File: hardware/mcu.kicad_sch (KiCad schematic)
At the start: 10 parts, among them U1 RP2350B

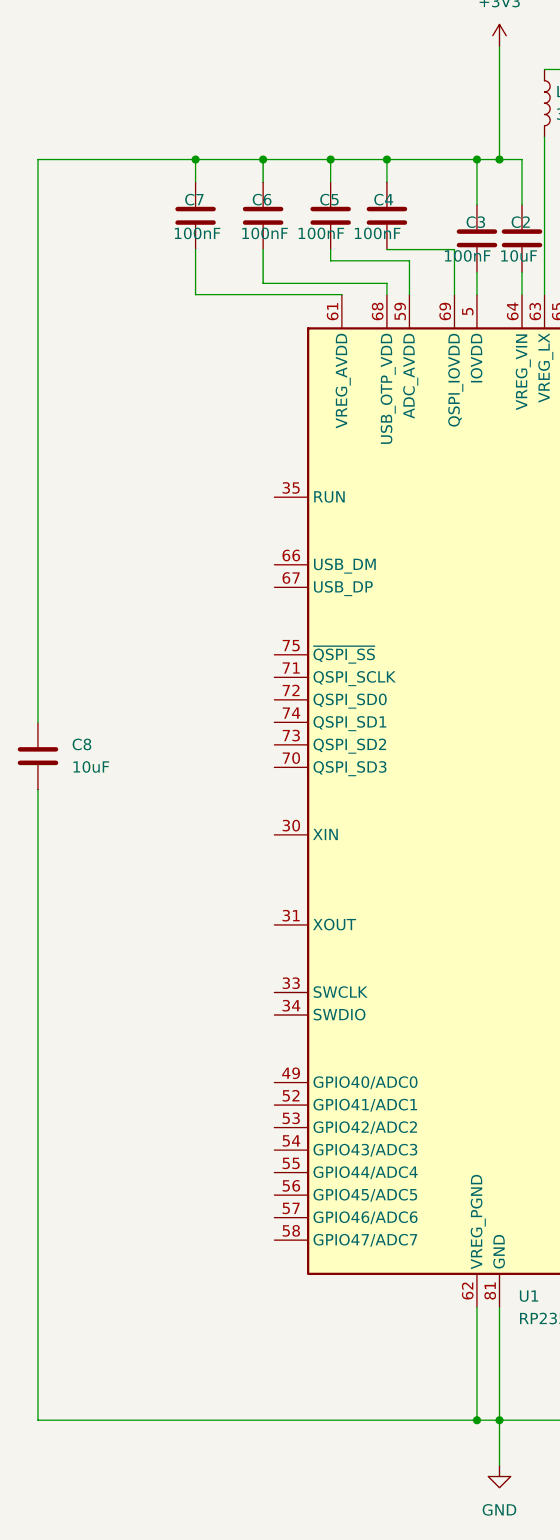
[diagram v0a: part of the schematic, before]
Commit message: add oscilator
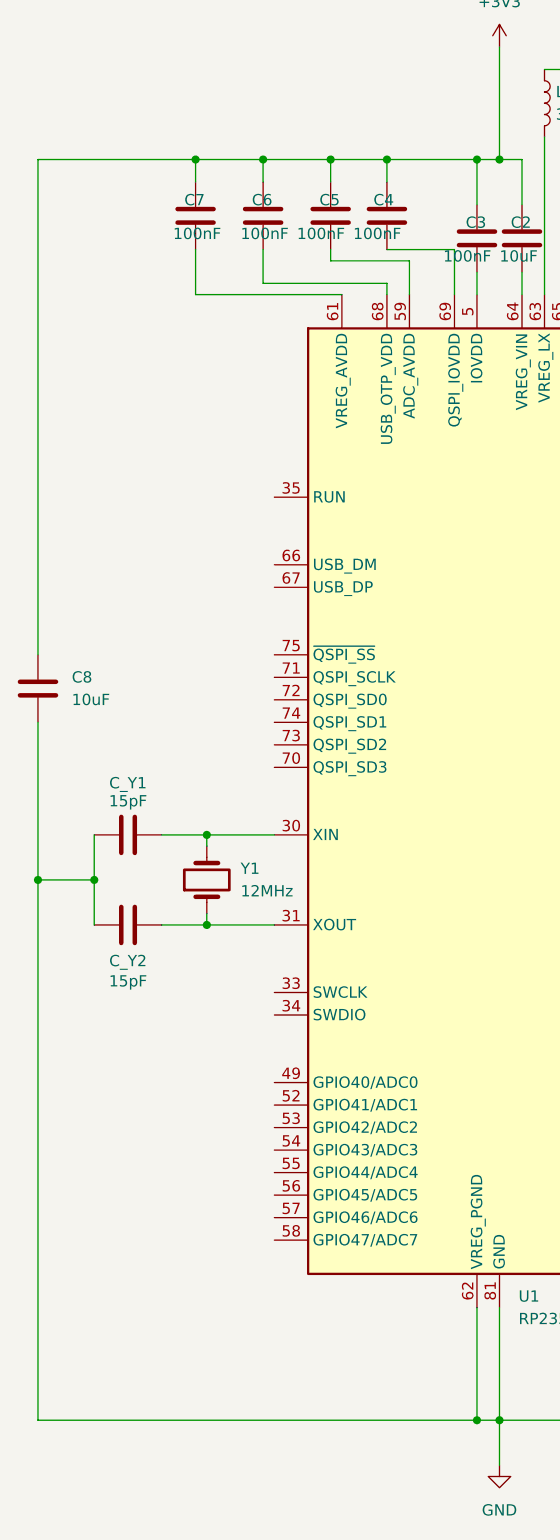
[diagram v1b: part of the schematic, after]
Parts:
- added C_Y1, C_Y2: 15pF, symbol Device:C
- added Y1: 12MHz, symbol Device:Crystal
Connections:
- net GND: now also C_Y1.1, C_Y2.1
- net at U1.30 (XIN): now also C_Y1.2, Y1.2
- net at U1.31 (XOUT): now also C_Y2.2, Y1.1
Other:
- moved on the sheet: C8

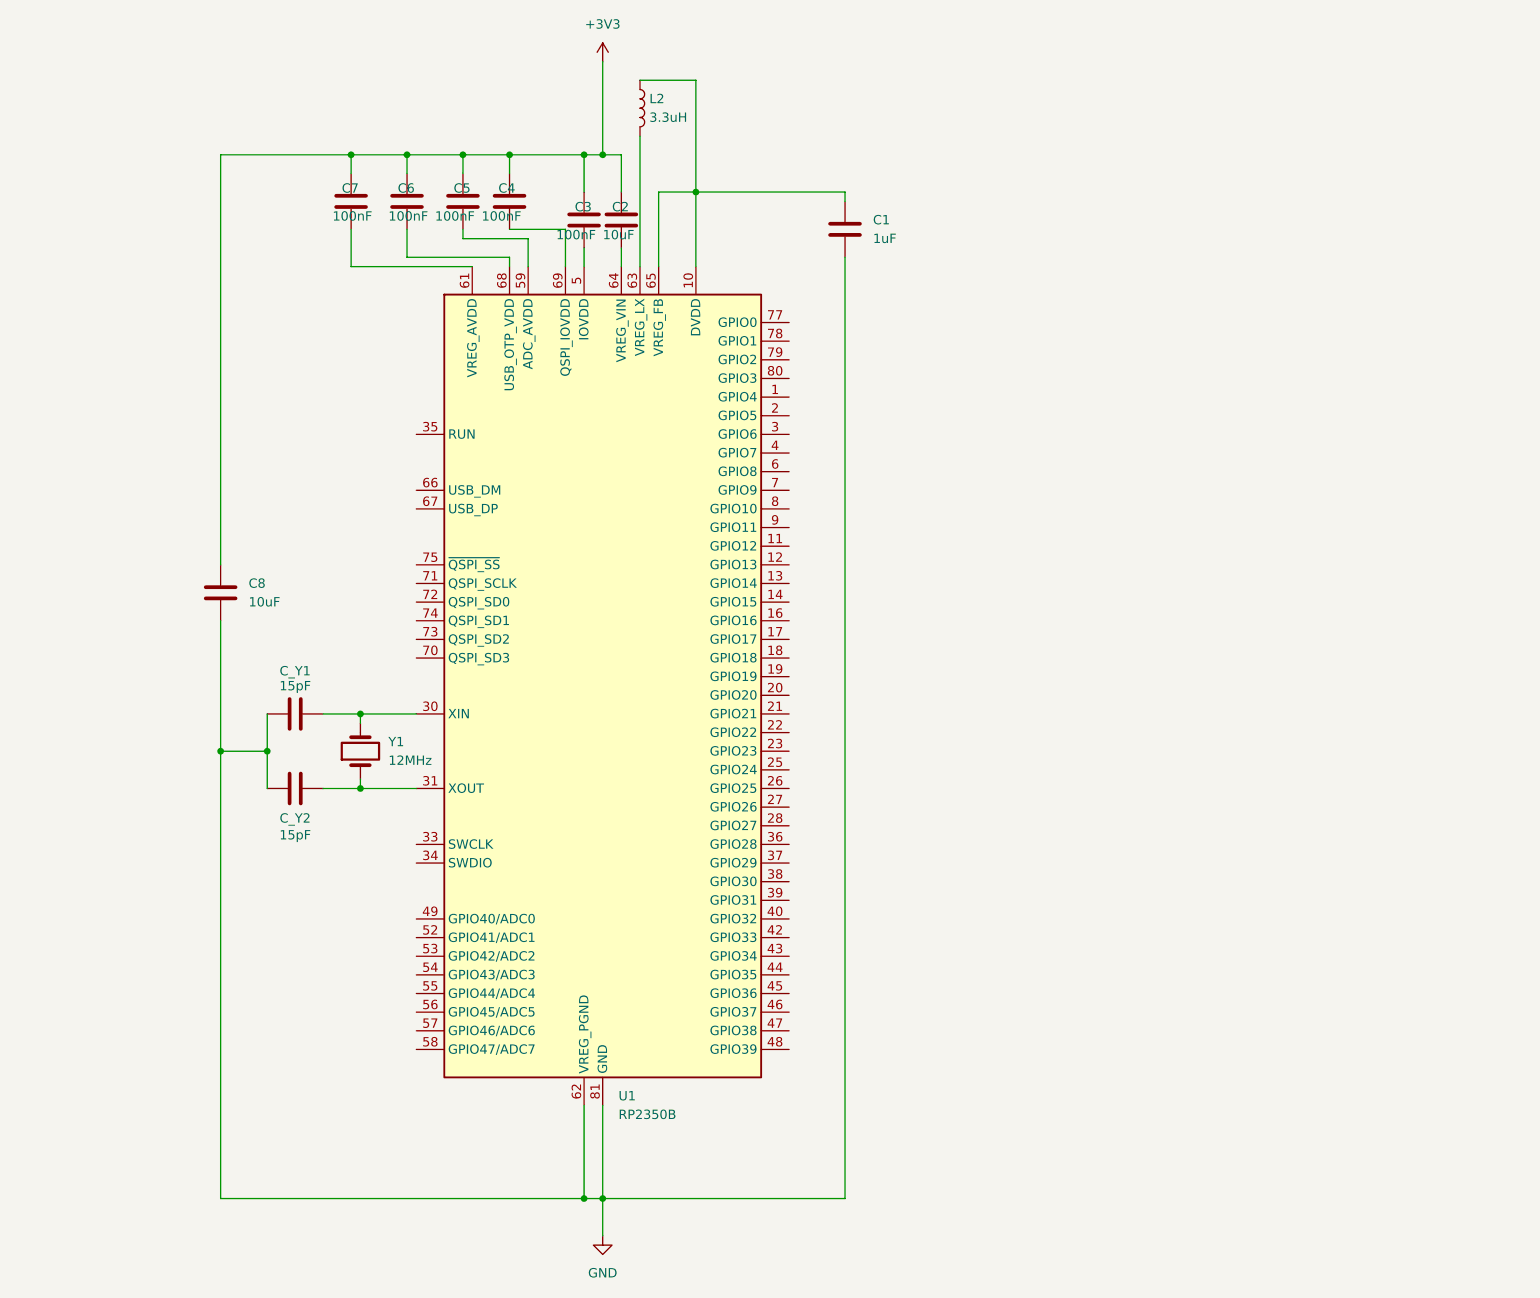
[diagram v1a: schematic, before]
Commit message: add flash reader
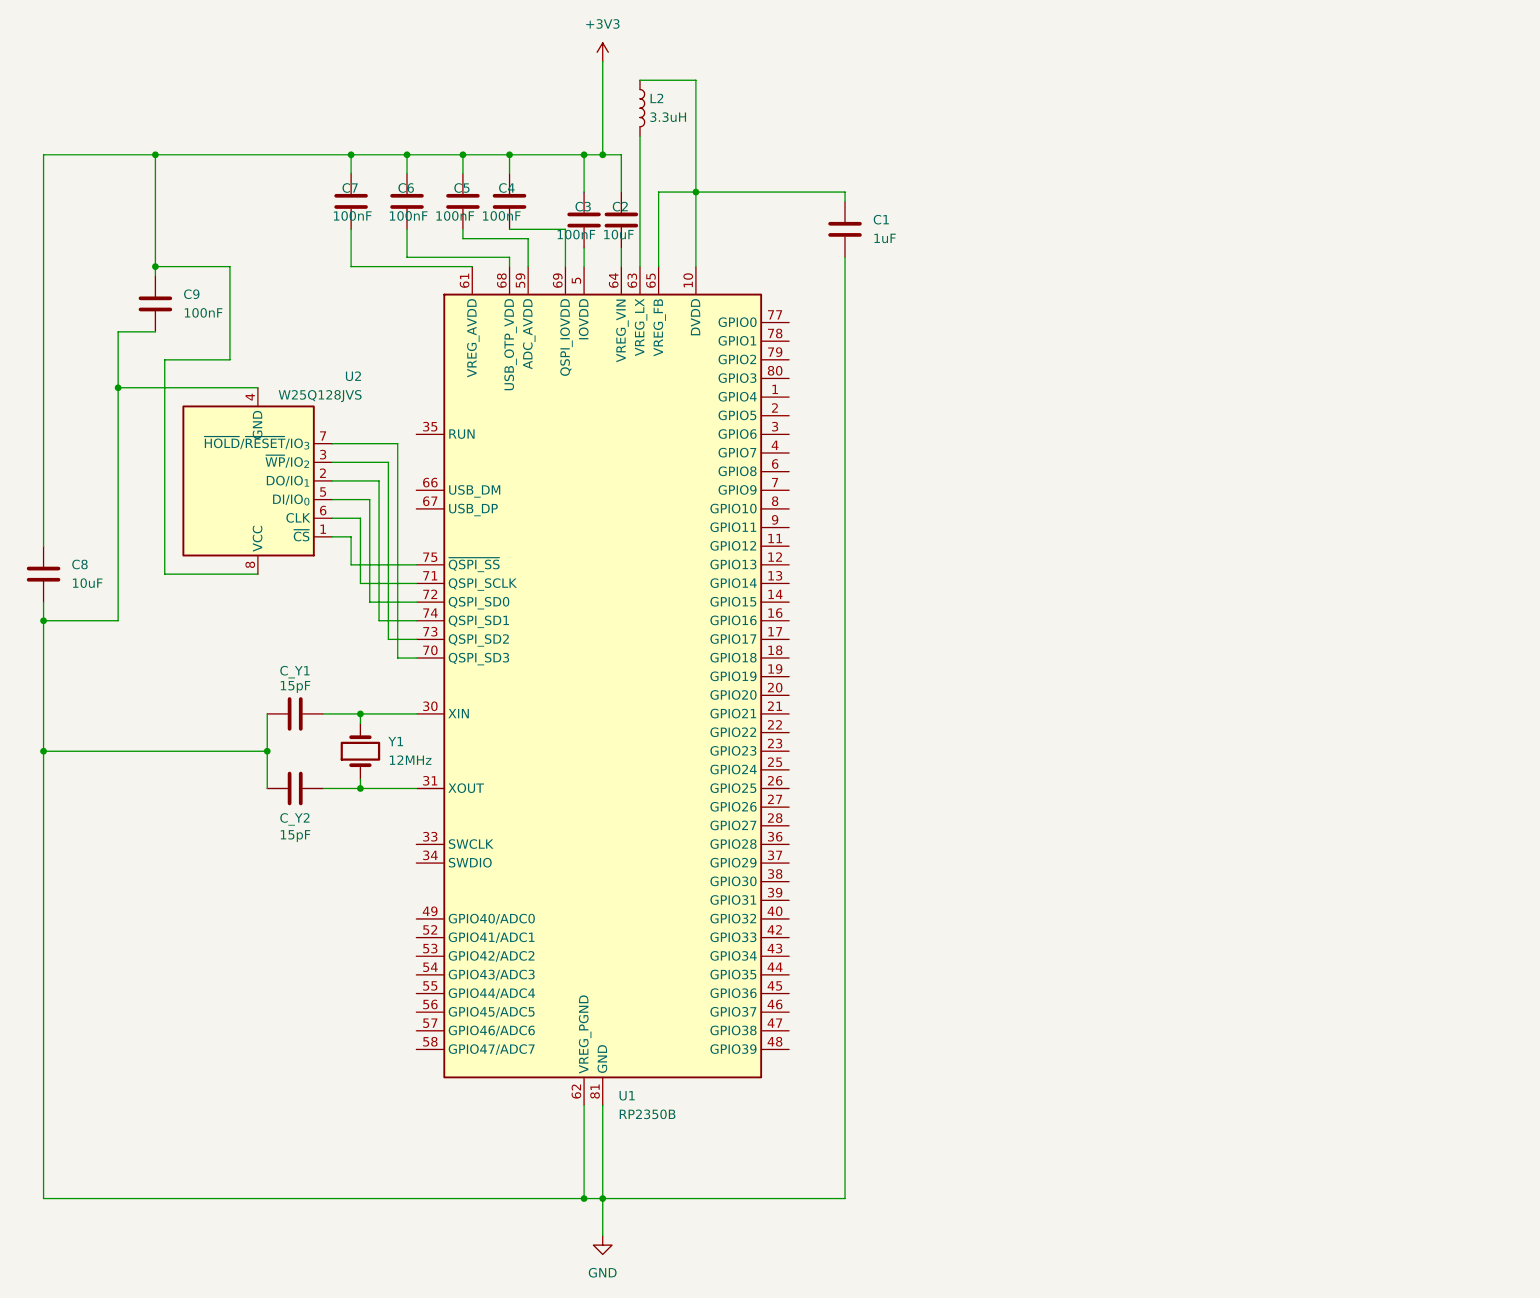
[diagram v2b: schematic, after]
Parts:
- added C9: 100nF, symbol Device:C
- added U2: W25Q128JVS, Package_SO:SOIC-8_5.3x5.3mm_P1.27mm, symbol Memory_Flash:W25Q128JVS
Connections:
- net +3V3: now also C9.1, U2.8 (VCC)
- net GND: now also C9.2, U2.4 (GND)
- net at U1.70 (QSPI_SD3): now also U2.7 (~{HOLD}/~{RESET}/IO_{3})
- net at U1.71 (QSPI_SCLK): now also U2.6 (CLK)
- net at U1.72 (QSPI_SD0): now also U2.5 (DI/IO_{0})
- net at U1.73 (QSPI_SD2): now also U2.3 (~{WP}/IO_{2})
- net at U1.74 (QSPI_SD1): now also U2.2 (DO/IO_{1})
- net at U1.75 (~{QSPI_SS}): now also U2.1 (~{CS})
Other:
- moved on the sheet: C8

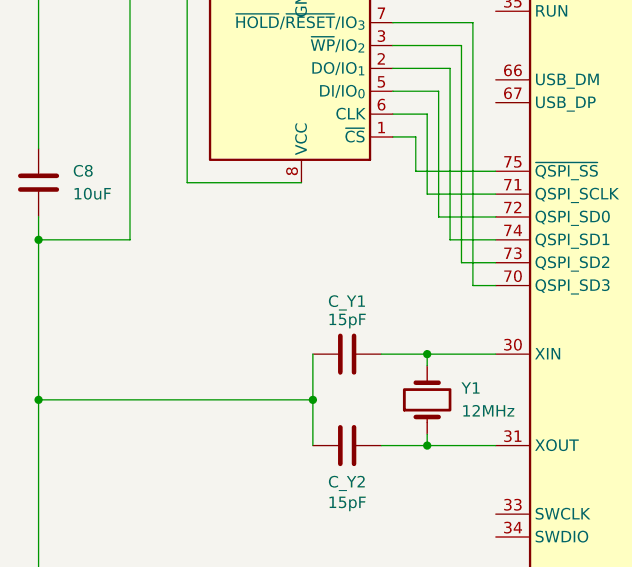
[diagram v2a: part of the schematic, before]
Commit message: add bootloader switch
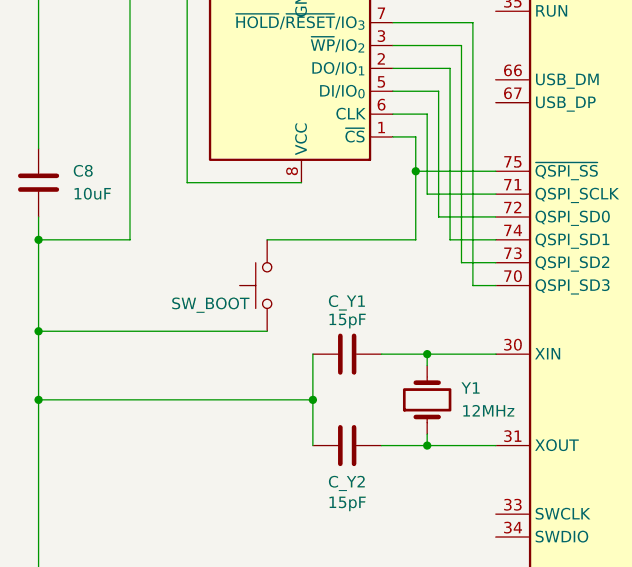
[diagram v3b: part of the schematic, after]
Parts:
- added SW_BOOT: SW_Push, symbol Switch:SW_Push
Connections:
- net GND: now also SW_BOOT.1
- net at U1.75 (~{QSPI_SS}), U2.1 (~{CS}): now also SW_BOOT.2
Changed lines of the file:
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@@
+	)
+	(junction
+		(at 21.59 109.22)
+		(diameter 0)
+		(color 0 0 0 0)
+	)
+	(junction
+		(at 63.5 91.44)
+		(diameter 0)
+		(color 0 0 0 0)
 	)
 	(junction
@@
 	(wire
 		(pts
+			(xy 21.59 109.22) (xy 46.99 109.22)
+		)
+		(stroke
+			(width 0)
+			(type default)
+		)
+	)
+	(wire
+		(pts
 			(xy 92.71 50.8) (xy 92.71 45.72)
 		)
@@
 	(wire
 		(pts
+			(xy 21.59 109.22) (xy 21.59 116.84)
+		)
+		(stroke
+			(width 0)
+			(type default)
+		)
+	)
+	(wire
+		(pts
 			(xy 63.5 38.1) (xy 63.5 35.56)
 		)
@@
 	(wire
 		(pts
-			(xy 21.59 99.06) (xy 21.59 116.84)
+			(xy 21.59 99.06) (xy 21.59 109.22)
 		)
 		(stroke
@@
 	(wire
 		(pts
+			(xy 63.5 99.06) (xy 63.5 91.44)
+		)
+		(stroke
+			(width 0)
+			(type default)
+		)
+	)
+	(wire
+		(pts
 			(xy 102.87 25.4) (xy 110.49 25.4)
+		)
+		(stroke
+			(width 0)
+			(type default)
+		)
+	)
+	(wire
+		(pts
+			(xy 46.99 99.06) (xy 63.5 99.06)
 		)
 		(stroke
@@
 					(unit 1)
 				)
+			)
+		)
+	)
+	(symbol
+		(lib_id "Switch:SW_Push")
+		(at 46.99 104.14 90)
+		(unit 1)
+		(exclude_from_sim no)
+		(in_bom yes)
+		(on_board yes)
+		(dnp no)
+		(property "Reference" "SW_BOOT"
+			(at 36.322 106.172 90)
+			(effects
+				(font
+					(size 1.27 1.27)
+				)
+				(justify right)
+			)
+		)
+		(property "Value" "SW_Push"
+			(at 36.322 105.41 90)
+			(effects
+				(font
+					(size 1.27 1.27)
+				)
+				(justify right)
+				(hide yes)
+			)
+		)
+		(property "Footprint" ""
+			(at 41.91 104.14 0)
+			(effects
+				(font
+					(size 1.27 1.27)
+				)
+				(hide yes)
+			)
+		)
+		(property "Datasheet" "~"
+			(at 41.91 104.14 0)
+			(effects
+				(font
+					(size 1.27 1.27)
+				)
+				(hide yes)
+			)
+		)
+		(property "Description" "Push button switch, generic, two pins"
+			(at 46.99 104.14 0)
+			(effects
+				(font
+					(size 1.27 1.27)
+				)
+				(hide yes)
+			)
+		)
+		(pin "1"
+		)
+		(pin "2"
+		)
+		(instances
+			(project ""
+				(path "/6bfeada4-0da3-4bdd-af4a-70929e466b35/1cd19f8e-9dd8-4d11-a3db-45fa5ed6d9f6"
+					(reference "SW_BOOT")
+					(unit 1)
+				)
